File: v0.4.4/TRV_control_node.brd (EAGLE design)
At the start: 65 x 30.7 mm, 48 parts, among them J3 AMP FCI 10103594-0001LF, J4 455-1750-1-ND, J6 AMP FCI 10103594-0001LF, SW1 EVQQ, SW2 EVQQ, U1 PCA9306, U11 915MHz, U2 FT231XQ-R, U5 ATMEGA328P-MU, U8 MCP1703/3.3V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

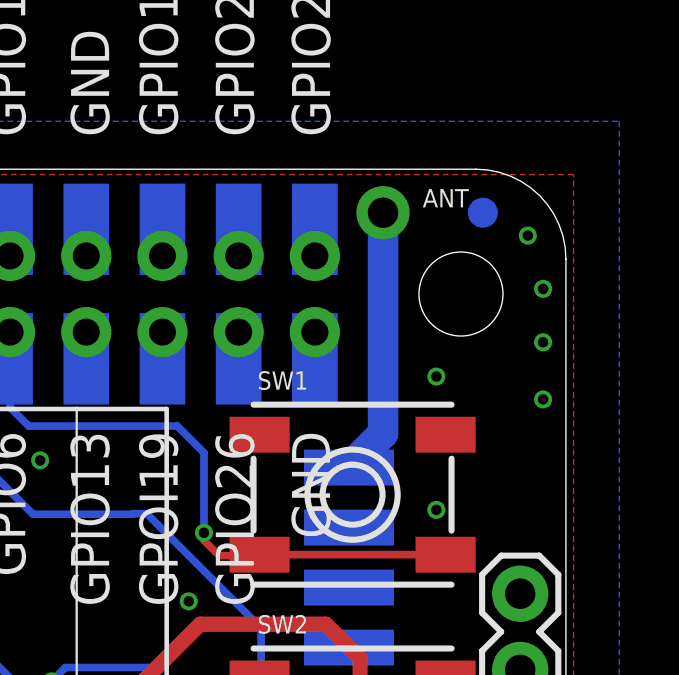
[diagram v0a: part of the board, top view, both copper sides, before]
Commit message: updated antenna trace
moved antenna pin header to the side to allow easy soldering
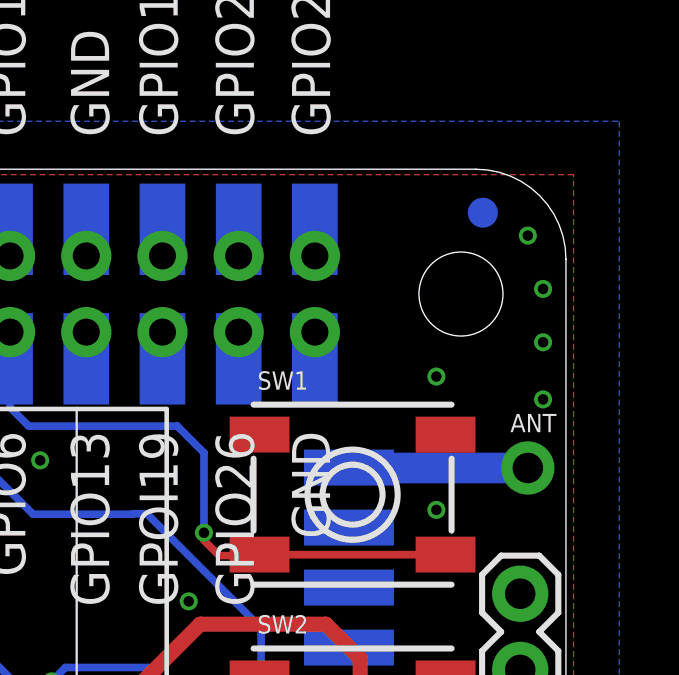
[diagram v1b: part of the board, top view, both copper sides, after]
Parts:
- moved ANT 9.78 mm to (63.8, 20.7)
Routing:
- net ANT: track 8.96 -> 5.97 mm
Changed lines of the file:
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@@
 <attribute name="VALUE" x="50.292" y="22.016" size="0.6096" layer="28" font="vector" ratio="20" rot="MR180" align="top-center"/>
 </element>
-<element name="ANT" library="adafruit@1" package="1X01-CLEANBIG" value="Antenna" x="58.928" y="29.21" smashed="yes">
-<attribute name="MPN" value="Helical antenna" x="58.928" y="29.21" size="1.778" layer="27" display="off"/>
-<attribute name="NAME" x="60.2488" y="29.3878" size="0.6096" layer="121" font="vector" ratio="10"/>
-<attribute name="VALUE" x="57.658" y="26.035" size="1.27" layer="27"/>
+<element name="ANT" library="adafruit@1" package="1X01-CLEANBIG" value="Antenna" x="63.754" y="20.701" smashed="yes">
+<attribute name="MPN" value="Helical antenna" x="63.754" y="20.701" size="1.778" layer="27" display="off"/>
+<attribute name="NAME" x="63.1698" y="21.8948" size="0.6096" layer="121" font="vector" ratio="10"/>
+<attribute name="VALUE" x="62.484" y="17.526" size="1.27" layer="27"/>
 </element>
 <element name="TC1" library="TagConnect" package="TC2030-IDC-NL" value="TC2030-IDC-NL" x="54.864" y="3.048" smashed="yes">
@@
 <contactref element="U11" pad="9"/>
 <contactref element="ANT" pad="1"/>
-<wire x1="57.792" y1="20.716" x2="58.928" y2="21.852" width="1.016" layer="16"/>
-<wire x1="58.928" y1="21.852" x2="58.928" y2="29.21" width="1.016" layer="16"/>
+<wire x1="63.754" y1="20.701" x2="57.807" y2="20.701" width="1.016" layer="16"/>
+<wire x1="57.807" y1="20.701" x2="57.792" y2="20.716" width="1.016" layer="16"/>
 </signal>
 <signal name="VIN">
